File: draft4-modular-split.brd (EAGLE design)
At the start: 100 x 100 mm, 28 parts, among them U2 SPX3819, X1 3v7 lipo, X2 ESP-12, X3 MOD-TP4056

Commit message: updates listed below
* used blossom battery case
* switched to 100uF big fat smds for "bulk" ws2812 support
* fixed values for vbat monitoring divider and added cap to hold it
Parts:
- removed C1: 100uF, microbuilder:_0805
- added C6, C7: 100uF, rcl:PANASONIC_B
- X1: device karls-parts-2016-09:KEYSTONE-1043 -> karls-parts-2016-09:BATT-18650-BLOSSOM-1
- moved X1 29.9 mm to (61.3, 10.7), flipped to the bottom
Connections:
- net GND: now also C6.-, C7.-
- net VBUS: now also C6.+, C7.+
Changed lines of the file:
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@@
 <element name="J1" library="SparkFun-Connectors" package="1X03_NO_SILK" value="" x="13.97" y="44.831"/>
 <element name="R1" library="resistor" package="R0603" value="470" x="-8.382" y="-220.472"/>
-<element name="X1" library="karls-parts-2016-09" package="KEYSTONE-1043" value="3v7 lipo" x="32.004" y="4.953"/>
+<element name="X1" library="karls-parts-2016-09" package="BATT-18650-BLOSSOM-1" value="3v7 lipo" x="61.34" y="10.668" locked="yes" rot="MR0"/>
 <element name="C3" library="microbuilder" package="_0805" value="100nF" x="6.477" y="65.024"/>
 <element name="C4" library="microbuilder" package="_0805" value="100nF" x="50.038" y="72.898"/>
@@
 <attribute name="PROD_ID" value=" SWCH-08441" x="39.37" y="42.926" size="1.778" layer="27" display="off"/>
 </element>
-<element name="C1" library="microbuilder" package="_0805" value="100uF" x="-19.431" y="-220.599"/>
 <element name="R2" library="resistor" package="R0603" value="10k" x="-19.939" y="-225.298"/>
 <element name="R3" library="resistor" package="R0603" value="10k" x="-19.939" y="-230.124"/>
+<element name="C6" library="rcl" package="PANASONIC_B" value="100uF" x="-20.828" y="-236.22"/>
+<element name="C7" library="rcl" package="PANASONIC_B" value="100uF" x="-20.828" y="-242.062"/>
 </elements>
 <signals>
@@
 <contactref element="S2" pad="1"/>
 <contactref element="R3" pad="1"/>
+<contactref element="C6" pad="-"/>
+<contactref element="C7" pad="-"/>
+<wire x1="-22.428" y1="-236.22" x2="-20.789" y2="-230.124" width="0" layer="19" extent="1-1"/>
+<wire x1="-22.428" y1="-242.062" x2="-22.428" y2="-236.22" width="0" layer="19" extent="1-1"/>
 <wire x1="-9.232" y1="-111.506" x2="-20.789" y2="-230.124" width="0" layer="19" extent="1-1"/>
 <wire x1="2.081" y1="2.16" x2="-9.232" y2="-111.506" width="0" layer="19" extent="1-1"/>
@@
 <wire x1="13.843" y1="11.43" x2="8.088" y2="13.909" width="0" layer="19" extent="1-1"/>
 <wire x1="19.0801" y1="14.986" x2="14.366" y2="11.69" width="0" layer="19" extent="1-1"/>
-<wire x1="23.844" y1="12.953" x2="19.0801" y2="14.986" width="0" layer="19" extent="1-1"/>
-<wire x1="28.177" y1="7.735" x2="23.844" y2="12.953" width="0" layer="19" extent="1-1"/>
+<wire x1="28.177" y1="7.735" x2="19.0801" y2="14.986" width="0" layer="19" extent="1-1"/>
 <wire x1="23.081" y1="2.16" x2="28.177" y2="7.735" width="0" layer="19" extent="1-1"/>
 <wire x1="57.792" y1="8.788" x2="28.177" y2="7.735" width="0" layer="19" extent="1-1"/>
@@
 <wire x1="25.0698" y1="45.0596" x2="13.97" y2="44.831" width="0" layer="19" extent="1-1"/>
 <wire x1="36.1188" y1="45.1866" x2="25.0698" y2="45.0596" width="0" layer="19" extent="1-1"/>
-<wire x1="1.37215625" y1="70.285028125" x2="13.97" y2="44.831" width="0" layer="19" extent="1-1"/>
-<wire x1="7.493" y1="65.024" x2="1.37215625" y2="70.285028125" width="0" layer="19" extent="1-1"/>
+<wire x1="7.493" y1="65.024" x2="13.97" y2="44.831" width="0" layer="19" extent="1-1"/>
 <wire x1="7.6" y1="72.577" x2="7.493" y2="65.024" width="0" layer="19" extent="1-1"/>
-<wire x1="51.054" y1="72.898" x2="7.6" y2="72.577" width="0" layer="19" extent="1-1"/>
+<wire x1="1.37215625" y1="70.285028125" x2="7.6" y2="72.577" width="0" layer="19" extent="1-1"/>
+<wire x1="51.054" y1="72.898" x2="36.1188" y2="45.1866" width="0" layer="19" extent="1-1"/>
 <wire x1="51.6" y1="80.577" x2="51.054" y2="72.898" width="0" layer="19" extent="1-1"/>
-<wire x1="93.599" y1="64.643" x2="51.6" y2="80.577" width="0" layer="19" extent="1-1"/>
-<wire x1="95.6" y1="72.577" x2="93.599" y2="64.643" width="0" layer="19" extent="1-1"/>
-<wire x1="98.62784375" y1="70.285028125" x2="95.6" y2="72.577" width="0" layer="19" extent="1-1"/>
+<wire x1="97.79" y1="10.668" x2="57.792" y2="8.788" width="0" layer="19" extent="1-1"/>
+<wire x1="93.599" y1="64.643" x2="51.054" y2="72.898" width="0" layer="19" extent="1-1"/>
+<wire x1="98.62784375" y1="70.285028125" x2="93.599" y2="64.643" width="0" layer="19" extent="1-1"/>
+<wire x1="95.6" y1="72.577" x2="98.62784375" y2="70.285028125" width="0" layer="19" extent="1-1"/>
 </signal>
 <signal name="VBUS">
@@
 <contactref element="U2" pad="3"/>
 <wire x1="18.266" y1="15.936" x2="19.0801" y2="15.936" width="0.254" layer="1"/>
-<wire x1="92.4" y1="67.423" x2="97.2" y2="62.8" width="0" layer="19" extent="1-1"/>
+<contactref element="C7" pad="+"/>
+<contactref element="C6" pad="+"/>
 <wire x1="91.567" y1="64.643" x2="92.4" y2="67.423" width="0" layer="19" extent="1-1"/>
+<wire x1="97.2" y1="62.8" x2="91.567" y2="64.643" width="0" layer="19" extent="1-1"/>
 <wire x1="49.022" y1="72.898" x2="91.567" y2="64.643" width="0" layer="19" extent="1-1"/>
 <wire x1="48.4" y1="75.423" x2="49.022" y2="72.898" width="0" layer="19" extent="1-1"/>
-<wire x1="4.4" y1="67.423" x2="48.4" y2="75.423" width="0" layer="19" extent="1-1"/>
-<wire x1="5.461" y1="65.024" x2="4.4" y2="67.423" width="0" layer="19" extent="1-1"/>
+<wire x1="5.461" y1="65.024" x2="48.4" y2="75.423" width="0" layer="19" extent="1-1"/>
+<wire x1="4.4" y1="67.423" x2="5.461" y2="65.024" width="0" layer="19" extent="1-1"/>
 <wire x1="2.8" y1="62.8" x2="5.461" y2="65.024" width="0" layer="19" extent="1-1"/>
-<wire x1="19.757" y1="18.796" x2="2.8" y2="62.8" width="0" layer="19" extent="1-1"/>
-<wire x1="19.0801" y1="15.936" x2="19.757" y2="18.796" width="0" layer="19" extent="1-1"/>
+<wire x1="2.081" y1="17.16" x2="2.8" y2="62.8" width="0" layer="19" extent="1-1"/>
+<wire x1="7.549" y1="12.009" x2="2.081" y2="17.16" width="0" layer="19" extent="1-1"/>
+<wire x1="18.266" y1="15.936" x2="8.088" y2="12.009" width="0" layer="19" extent="1-1"/>
 <wire x1="19.0801" y1="14.036" x2="19.0801" y2="15.936" width="0" layer="19" extent="1-1"/>
-<wire x1="8.088" y1="12.009" x2="18.266" y2="15.936" width="0" layer="19" extent="1-1"/>
-<wire x1="2.081" y1="17.16" x2="7.549" y2="12.009" width="0" layer="19" extent="1-1"/>
+<wire x1="19.757" y1="18.796" x2="19.0801" y2="15.936" width="0" layer="19" extent="1-1"/>
+<wire x1="-19.228" y1="-236.22" x2="7.549" y2="12.009" width="0" layer="19" extent="1-1"/>
+<wire x1="-19.228" y1="-242.062" x2="-19.228" y2="-236.22" width="0" layer="19" extent="1-1"/>
 </signal>
 <signal name="VBAT">
@@
 <wire x1="23.081" y1="17.16" x2="-19.089" y2="-225.298" width="0" layer="19" extent="1-1"/>
 <wire x1="16.057" y1="18.796" x2="23.081" y2="17.16" width="0" layer="19" extent="1-1"/>
-<wire x1="95.484" y1="12.953" x2="23.081" y2="17.16" width="0" layer="19" extent="1-1"/>
+<wire x1="24.89" y1="10.668" x2="23.081" y2="17.16" width="0" layer="19" extent="1-1"/>
 </signal>
 <signal name="3.3V">

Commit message: Routed all basic signals
Going to hold here and use all that space to put in the pfet+diode
method as well as just optional footprints.

only get one build
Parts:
- removed R2, R3: 10k, resistor:R0603
- added C31: 100nF, microbuilder:_0805
- added R31: 470k, resistor:R0603
- added R32: 100k, resistor:R0603
- moved C7 322.2 mm to (91.9, 59.8)
- moved C6 298.5 mm to (8.46, 60.8), turned to 180 degrees
- moved R1 279.7 mm to (3.31, 59.0)
- moved R14 239.8 mm to (56.7, 34.0)
- moved R15 191.4 mm to (31.5, 41.9), turned to 180 degrees
- moved R12 155.5 mm to (56.8, 29.7), turned to 180 degrees
- moved R13 155.4 mm to (60.4, 32.7), turned to 90 degrees
- moved R11 145.3 mm to (31.4, 37.9), turned to 180 degrees
- moved S1 46.9 mm to (75.1, 40.9), turned to 90 degrees
- moved J1 46.6 mm to (60.2, 38.9), turned to 90 degrees
- moved S2 27.6 mm to (66.9, 40.9), turned to 90 degrees
- moved X2 20.1 mm to (44.1, 36.1)
- moved C23 18.7 mm to (12.1, 18.1), turned to 0 degrees
- moved D21 7.11 mm to (17.8, 11.7), turned to 0 degrees
- moved U2 6.25 mm to (12.2, 12.2), turned to 0 degrees
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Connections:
- net BAT_MON: now also C31.1, R31.1, R32.2; no longer R2.1, R3.2
- net GND: now also C31.2, R32.1; no longer R3.1
- net VBAT: now also R31.2; no longer R2.2
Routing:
- net GPIO2: track 0.00 -> 87.9 mm
- net VBUS: track 1.35 -> 52.5 mm, vias 0 -> 1
- net D4_IN: track 0.00 -> 50.2 mm
- net RESET: track 0.00 -> 49.2 mm, vias 0 -> 1
- net D5_IN: track 0.00 -> 47.9 mm
- net BAT_MON: track 0.00 -> 37.6 mm
- net GPIO0: track 0.00 -> 20.5 mm, vias 0 -> 1
- net GND: track 0.70 -> 13.0 mm
- net VBAT: track 0.00 -> 10.3 mm
- net TXD: track 0.00 -> 9.48 mm
- net RXD: track 0.00 -> 9.26 mm
- net RIGHT_IN: track 0.00 -> 8.14 mm
- net D3_IN: track 0.00 -> 7.90 mm
- net LEFT_IN: track 0.00 -> 7.63 mm
- net GPIO15: track 0.00 -> 4.44 mm
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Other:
- board size 100 x 100 mm -> 100 x 85 mm

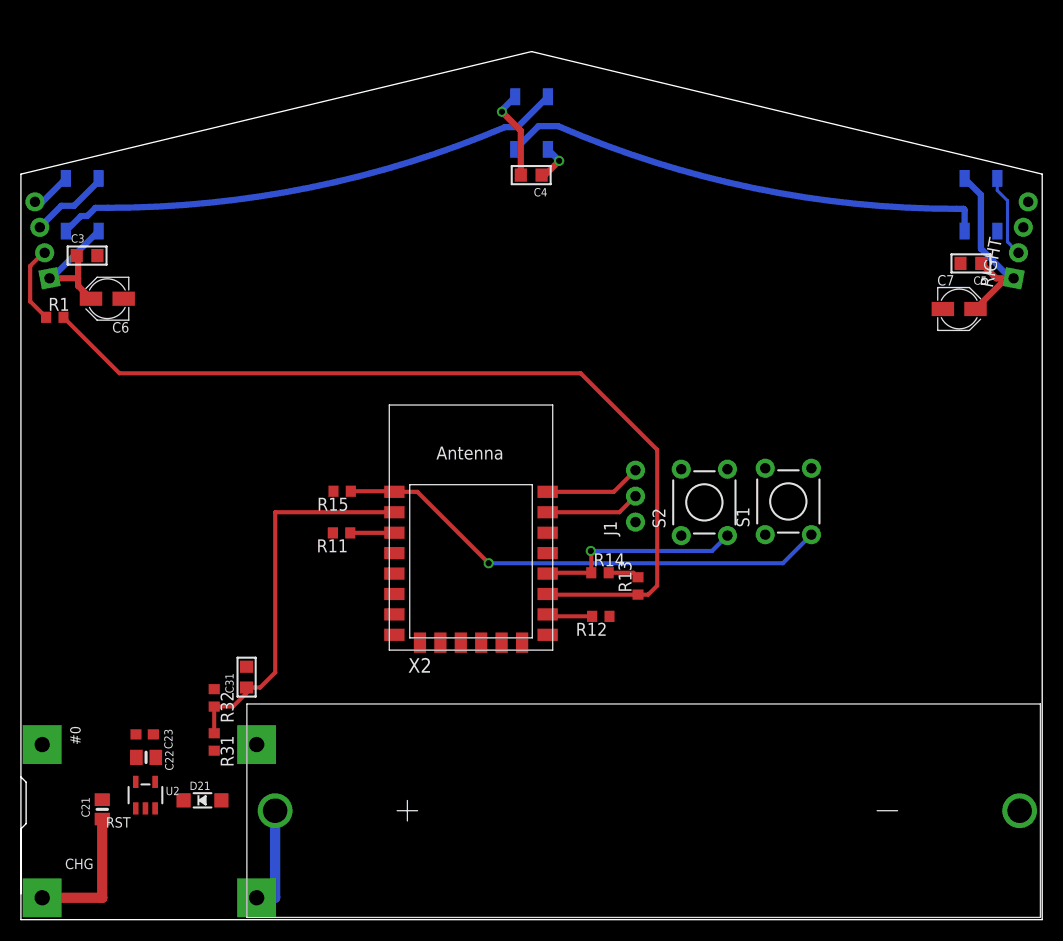
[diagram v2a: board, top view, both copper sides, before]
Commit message: added optional pfet+diode power path instead of diode
fully routed, corrected error with (non)rotated wings.
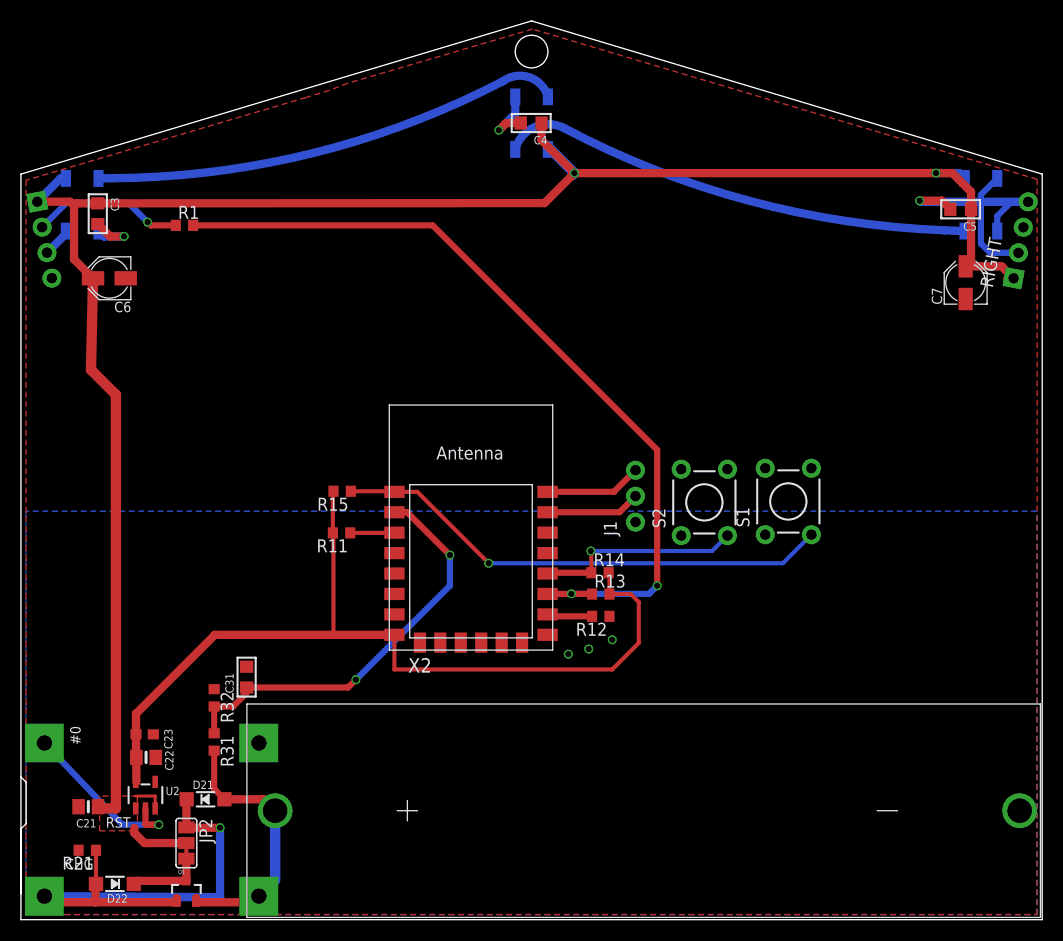
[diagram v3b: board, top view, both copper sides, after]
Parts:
- added D22: MBR120, microbuilder:SOD-123
- added JP2: (no value), SparkFun-Passives:PAD-JUMPER-3-2OF3_NC_BY_TRACE_YES_SILK_LARGE
- added Q1: (no value), SparkFun-DiscreteSemi:SOT23-3
- added R21: 470k, resistor:R0603
- moved R1 15.6 mm to (16.0, 68.0)
- moved LEFT 7.60 mm to (1.60, 70.3), turned to 259.2 degrees
- moved C5 5.39 mm to (92.0, 69.6)
- moved C4 5.10 mm to (50.0, 78.0)
- moved C3 4.23 mm to (7.52, 69.1), turned to 270 degrees
- moved R13 3.73 mm to (56.8, 31.9), turned to 0 degrees
- moved C7 2.65 mm to (92.5, 62.4), turned to 90 degrees
- moved C6 2.01 mm to (8.66, 62.8)
- moved C21 1.39 mm to (6.60, 11.1), turned to 180 degrees
- moved D21 0.32 mm to (18.1, 11.8)
- moved X3 0.27 mm to (13.3, 9.30)
- turned D3 to 270 degrees
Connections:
- new net N$3: D22.C, JP2.3, Q1.3
- new net VSYS: C21.1, C3.1, C4.1, C5.1, C6.+, C7.+, D3.1, D4.1, D5.1, JP2.2, LEFT.1, RIGHT.1, U2.1, U2.3
- net GND: now also R21.2
- net VBAT: now also Q1.2
- net VBUS: now also D22.A, JP2.1, Q1.1, R21.1; no longer C21.1, C3.1, C4.1, C5.1, C6.+, C7.+, D3.1, D4.1, D5.1, LEFT.1, RIGHT.1, U2.1, U2.3
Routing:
- net VSYS: track 0.00 -> 196.2 mm, vias 0 -> 2
- net 3.3V: track 3.06 -> 87.1 mm
- net GND: track 13.0 -> 48.8 mm, vias 1 -> 7
- net VBAT: track 10.3 -> 26.5 mm
- net N$3: track 0.00 -> 7.45 mm
- net LEFT_IN: track 7.63 -> 15.0 mm, vias 0 -> 1
- net GPIO2: track 87.9 -> 81.0 mm, vias 0 -> 2
- net D3_IN: track 7.90 -> 2.88 mm
- net D4_IN: track 50.2 -> 45.4 mm
- net VBUS: track 52.5 -> 48.8 mm
- net BAT_MON: track 37.6 -> 41.1 mm, vias 0 -> 2
- net RIGHT_IN: track 8.14 -> 11.1 mm
- net D5_IN: track 47.9 -> 45.8 mm
- added copper zone on layer 1, net GND
- added copper zone on layer 16, net GND
- added copper zone on layer 1, net VSYS
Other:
- board size 100 x 85 mm -> 100 x 88 mm
